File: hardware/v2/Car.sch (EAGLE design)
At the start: 64 parts

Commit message: Swapped non-analog input pins for ones that do support analog input. Significantly cleaned up schematic.
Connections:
- net N$12 renamed D0
- net N$19 renamed M2_V2
- net N$21 renamed M1_V2
- net N$23 renamed M1_I0X
- net N$25 renamed MOSI
- net N$26 renamed MISO
- net N$28 renamed PGC
- net N$3 renamed PGD
- net N$30 renamed M1_V1
- net N$38 renamed M2_V1
- net N$39 renamed D1
- net N$43 renamed D2
- net N$44 renamed D3
- net N$47 renamed D4
- net N$48 renamed D5
- net N$49 renamed D6
- net N$50 renamed D7
- net N$56 renamed M1_I1X
- net N$60 renamed M2_I0X
- net N$61 renamed M2_I1X
- net N$62 renamed M1_P1
- net N$63 renamed M1_P2
- net N$66 renamed M2_P1
- net N$67 renamed M2_P2
- net N$7 renamed SCLK
- net VCCIO renamed /RST
- removed net N$22: BRAINS.RB14/CN12, MOUTH.NSEL
- removed net N$24: BRAINS.RB15/CN11, MOUTH.NIRQ
- removed net N$29: AIO.5, BRAINS.RA2/CN30
- removed net N$32: AIO.6, BRAINS.RA3/CN29
- removed net N$36: ARMS./CS, BRAINS.RB12/CN14, M.ARMS./CS
- removed net N$37: ARMS.INT, BRAINS.RB13/CN13
- removed net N$45: AIO.3, BRAINS.RA0/CN2, HB.A
- removed net N$53: AIO.4, BRAINS.RA1/CN3
- removed net N$54: AIO.8, BRAINS.RB2/CN6
- removed net N$55: AIO.9, BRAINS.RB3/CN7
- removed net N$57: AIO.7, BRAINS.RA4/CN0
- removed net N$59: AIO.10, BRAINS.RB4/CN1
- new net A0: AIO.3, BRAINS.RB2/CN6
- new net A1: AIO.4, BRAINS.RB3/CN7
- new net A2: AIO.5, BRAINS.RB4/CN1
- new net A3: AIO.6, BRAINS.RB12/CN14
- new net A4: AIO.7, BRAINS.RB13/CN13
- new net A5: AIO.8, BRAINS.RB14/CN12
- new net A6: AIO.9, BRAINS.RB15/CN11
- new net A7: AIO.10, BRAINS.RA0/CN2, HB.A
- new net DIO_CS: ARMS./CS, BRAINS.RA4/CN0, M.ARMS./CS
- new net DIO_IRQ: ARMS.INT, BRAINS.RA3/CN29
- new net RFM_CS: BRAINS.RA2/CN30, MOUTH.NSEL
- new net RFM_IRQ: BRAINS.RA1/CN3, MOUTH.NIRQ
- net +3V3: now also PWR.A
- net +5V: no longer PWR.A
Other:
- moved on the sheet: 11CC, 11CT, 11RC, 11RP, 11RS, 11RT, 12CC, 12CT, 12RC, 12RP, 12RS, 12RT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

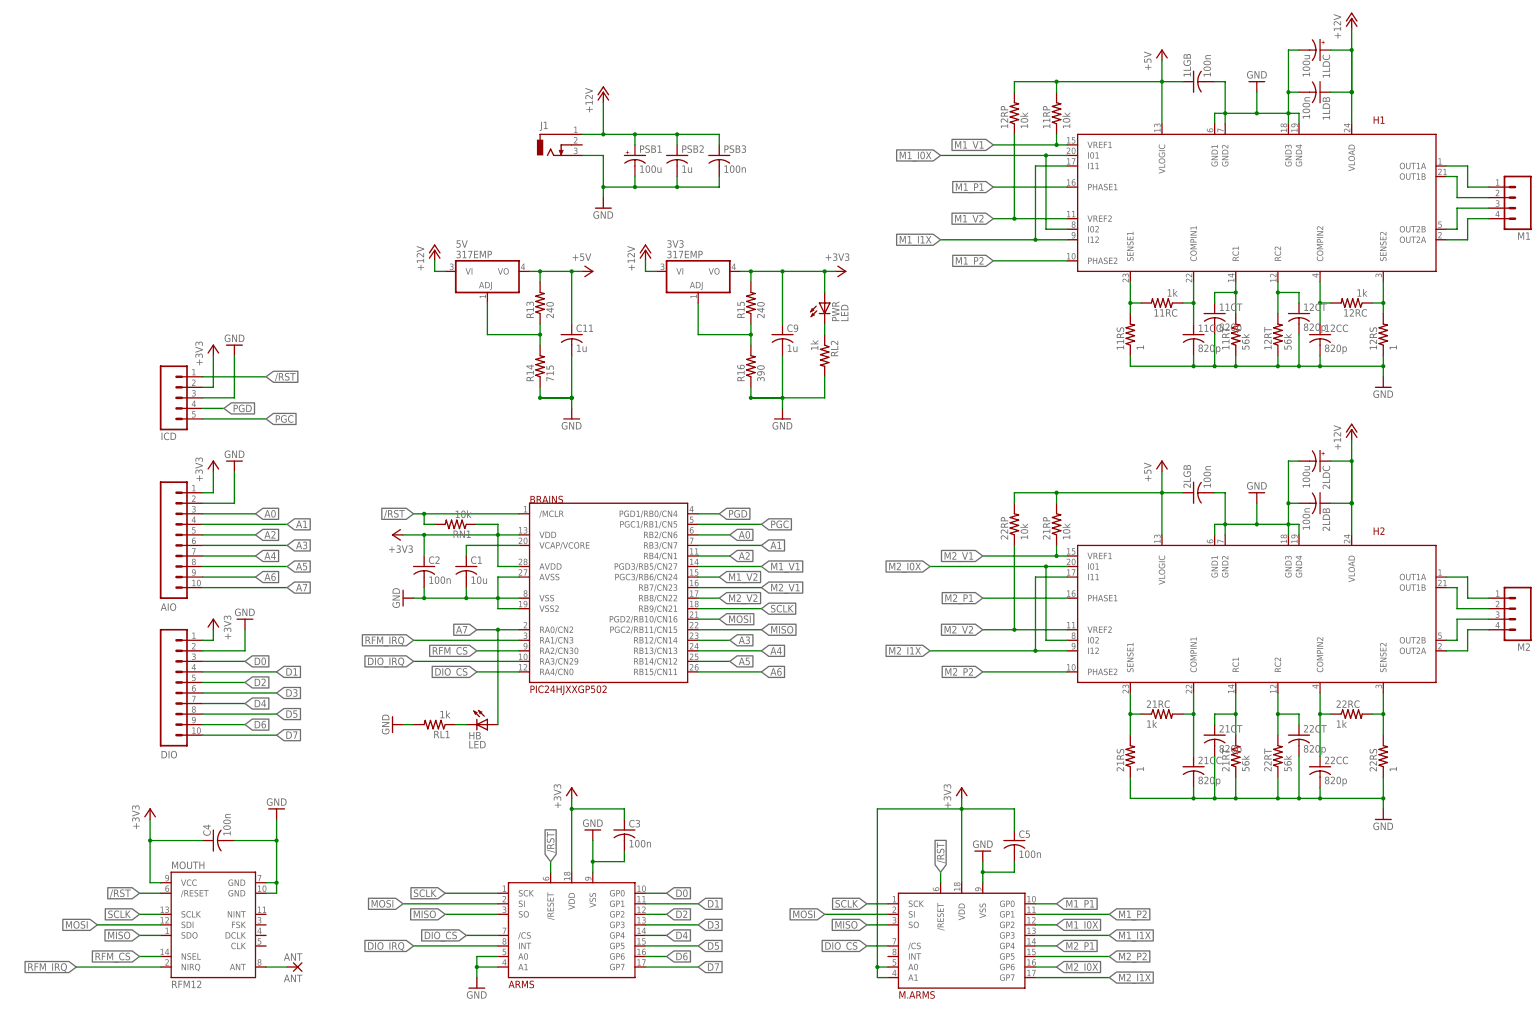
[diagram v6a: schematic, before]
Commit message: More schematic and layout cleanup.
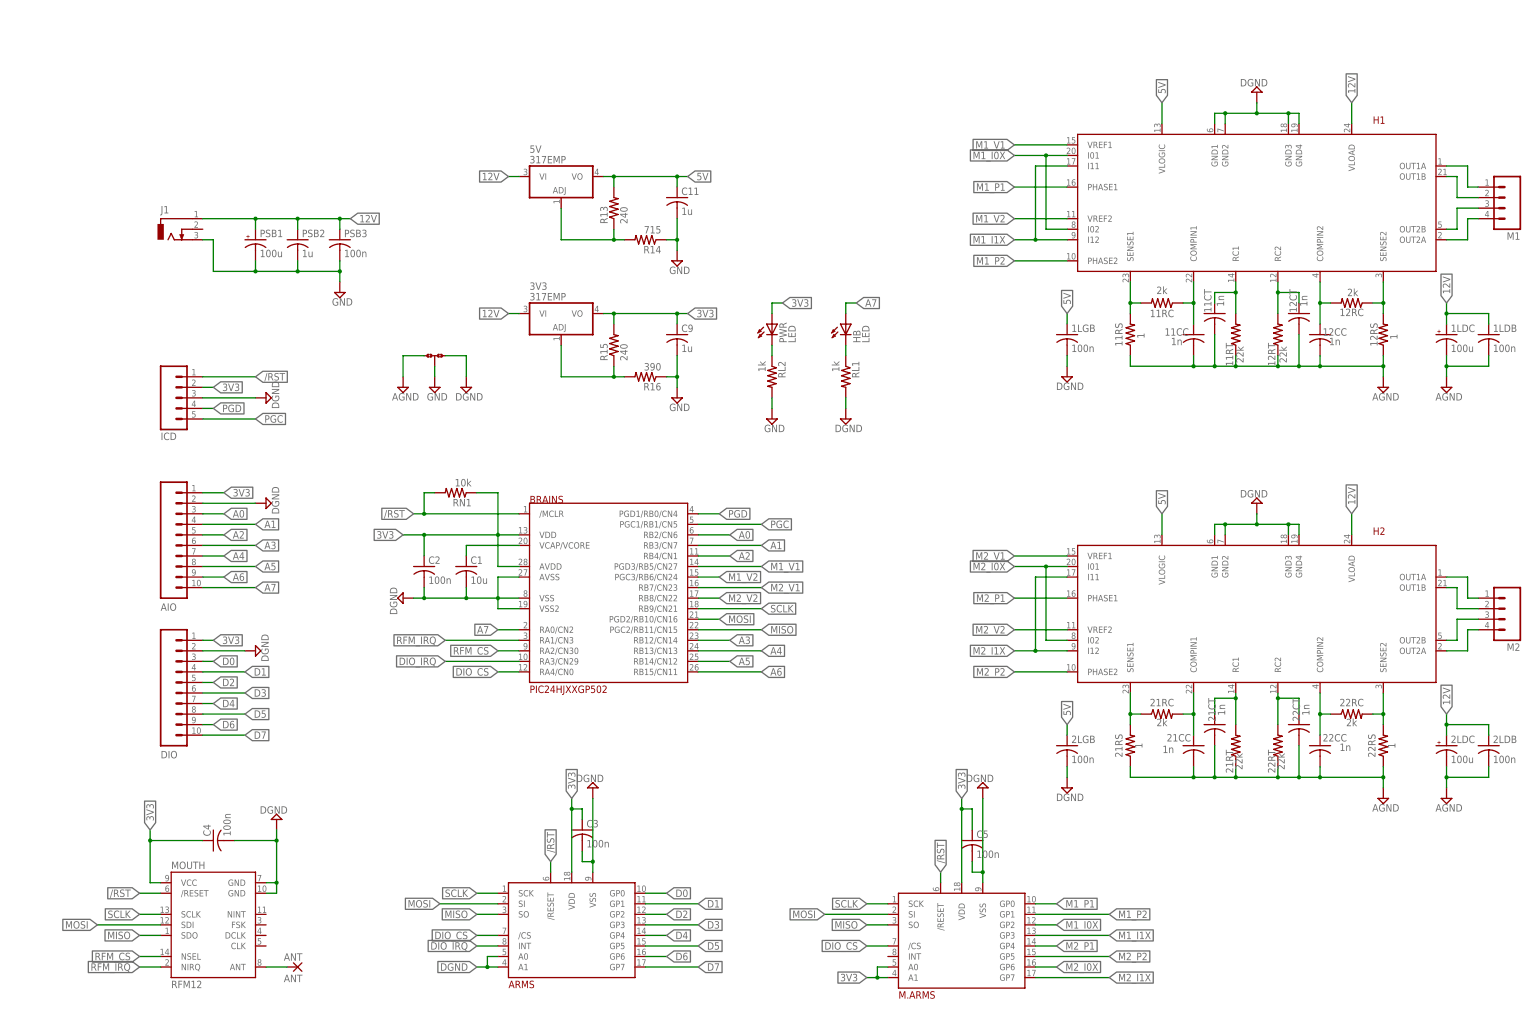
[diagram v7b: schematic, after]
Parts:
- removed 11RP, 12RP, 21RP, 22RP: 10k, rcl:R-US_R0805
- added JMP1: 0R-JUMPC, jump-0r-smd:0R-JUMPC
- 11CC, 11CT, 12CC, 12CT, 21CC, 21CT, 22CC, 22CT: value 820p -> 1n
- 11RC, 12RC, 21RC, 22RC: value 1k -> 2k
- 11RT, 12RT, 21RT, 22RT: value 56k -> 22k
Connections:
- net +12V renamed 12V
- net +3V3 renamed 3V3
- removed net +5V: 11RP.2, 12RP.2, 1LGB.1, 21RP.2, 22RP.2, 2LGB.1, 5V.VO, C11.1, H1.VLOGIC, H2.VLOGIC, R13.2
- new net 5V: 1LGB.1, 2LGB.1, 5V.VO, C11.1, H1.VLOGIC, H2.VLOGIC, R13.2
- new net AGND: 11CC.2, 11CT.2, 11RS.1, 11RT.1, 12CC.2, 12CT.2, 12RS.1, 12RT.1, 1LDB.2, 1LDC.-, 21CC.2, 21CT.2, 21RS.1, 21RT.1, 22CC.2, 22CT.2, 22RS.1, 22RT.1, 2LDB.2, 2LDC.-, JMP1-0R.3
- new net DGND: 1LGB.2, 2LGB.2, AIO.2, ARMS.A0, ARMS.A1, ARMS.VSS, BRAINS.AVSS, BRAINS.VSS, BRAINS.VSS2, C1.2, C2.2, C3.2, C4.2, C5.2, DIO.2, H1.GND1, H1.GND2, H1.GND3, H1.GND4, H2.GND1, H2.GND2, H2.GND3, H2.GND4, ICD.3, JMP1-0R.1, M.ARMS.VSS, MOUTH.GND@1, MOUTH.GND@2, RL1.2
- net GND: now also JMP1-0R.2; no longer 11CC.2, 11CT.2, 11RS.1, 11RT.1, 12CC.2, 12CT.2, 12RS.1, 12RT.1, 1LDB.2, 1LDC.-, 1LGB.2, 21CC.2, 21CT.2, 21RS.1, 21RT.1, 22CC.2, 22CT.2, 22RS.1, 22RT.1, 2LDB.2, 2LDC.-, 2LGB.2, AIO.2, ARMS.A0, ARMS.A1, ARMS.VSS, BRAINS.AVSS, BRAINS.VSS, BRAINS.VSS2, C1.2, C2.2, C3.2, C4.2, C5.2, DIO.2, H1.GND1, H1.GND2, H1.GND3, H1.GND4, H2.GND1, H2.GND2, H2.GND3, H2.GND4, ICD.3, M.ARMS.VSS, MOUTH.GND@1, MOUTH.GND@2, RL1.2
- net M1_V1: no longer 11RP.1
- net M1_V2: no longer 12RP.1
- net M2_V1: no longer 21RP.1
- net M2_V2: no longer 22RP.1
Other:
- moved on the sheet: 1LDB, 1LDC, 1LGB, 21CC, 21CT, 21RS, 21RT, 22CC, 22CT, 22RS, 22RT, 2LDB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

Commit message: Adding low pass filters to PWM outputs (for motor VREF).
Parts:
- removed JMP1: 0R-JUMPC, jump-0r-smd:0R-JUMPC
- added CA, CB: 1n, rcl:C-USC0805
- added RA, RB, RFA, RFB, RGA, RGB: 2k, rcl:R-US_R0805
- added SJ1, SJ2: (no value), jumper:SJ
- added U$1, U$2: MCP6L2-X_SN, microchip2:MCP6L2-X_SN
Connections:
- new net M1_PWM1: BRAINS.PGD3/RB5/CN27, RA.2
- new net M1_PWM2: BRAINS.PGC3/RB6/CN24, RB.2
- new net M2_PWM1: BRAINS.RB7/CN23
- new net M2_PWM2: BRAINS.RB8/CN22
- new net N$21: RFB.2, U$1.VINB-
- new net N$22: CB.1, RB.1, U$1.VINB+
- new net N$3: CA.1, RA.1, U$1.VINA+
- new net N$7: RFA.2, U$1.VINA-
- net 5V: now also U$1.VDD
- net AGND: now also CA.2, CB.2, RGA.2, RGB.2, SJ1.1, U$1.VSS; no longer JMP1-0R.3
- net DGND: now also SJ2.2; no longer JMP1-0R.1
- net GND: now also SJ1.2, SJ2.1; no longer JMP1-0R.2
- net M1_V1: now also RFA.1, RGA.1, U$1.VOUTA; no longer BRAINS.PGD3/RB5/CN27
- net M1_V2: now also RFB.1, RGB.1, U$1.VOUTB; no longer BRAINS.PGC3/RB6/CN24
- net M2_V1: no longer BRAINS.RB7/CN23
- net M2_V2: no longer BRAINS.RB8/CN22
